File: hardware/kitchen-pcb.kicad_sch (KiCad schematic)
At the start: 51 parts, among them J1 MEM2075-00-140-01-A, J2 Conn_02x02_Odd_Even, J3 Conn_01x06, J4 S3B-XH-SM4-TB_LF__SN_, Q1 TEMT6000X01, U1 SHT30-DIS-B, U2 MX25L3233FM2I-08G

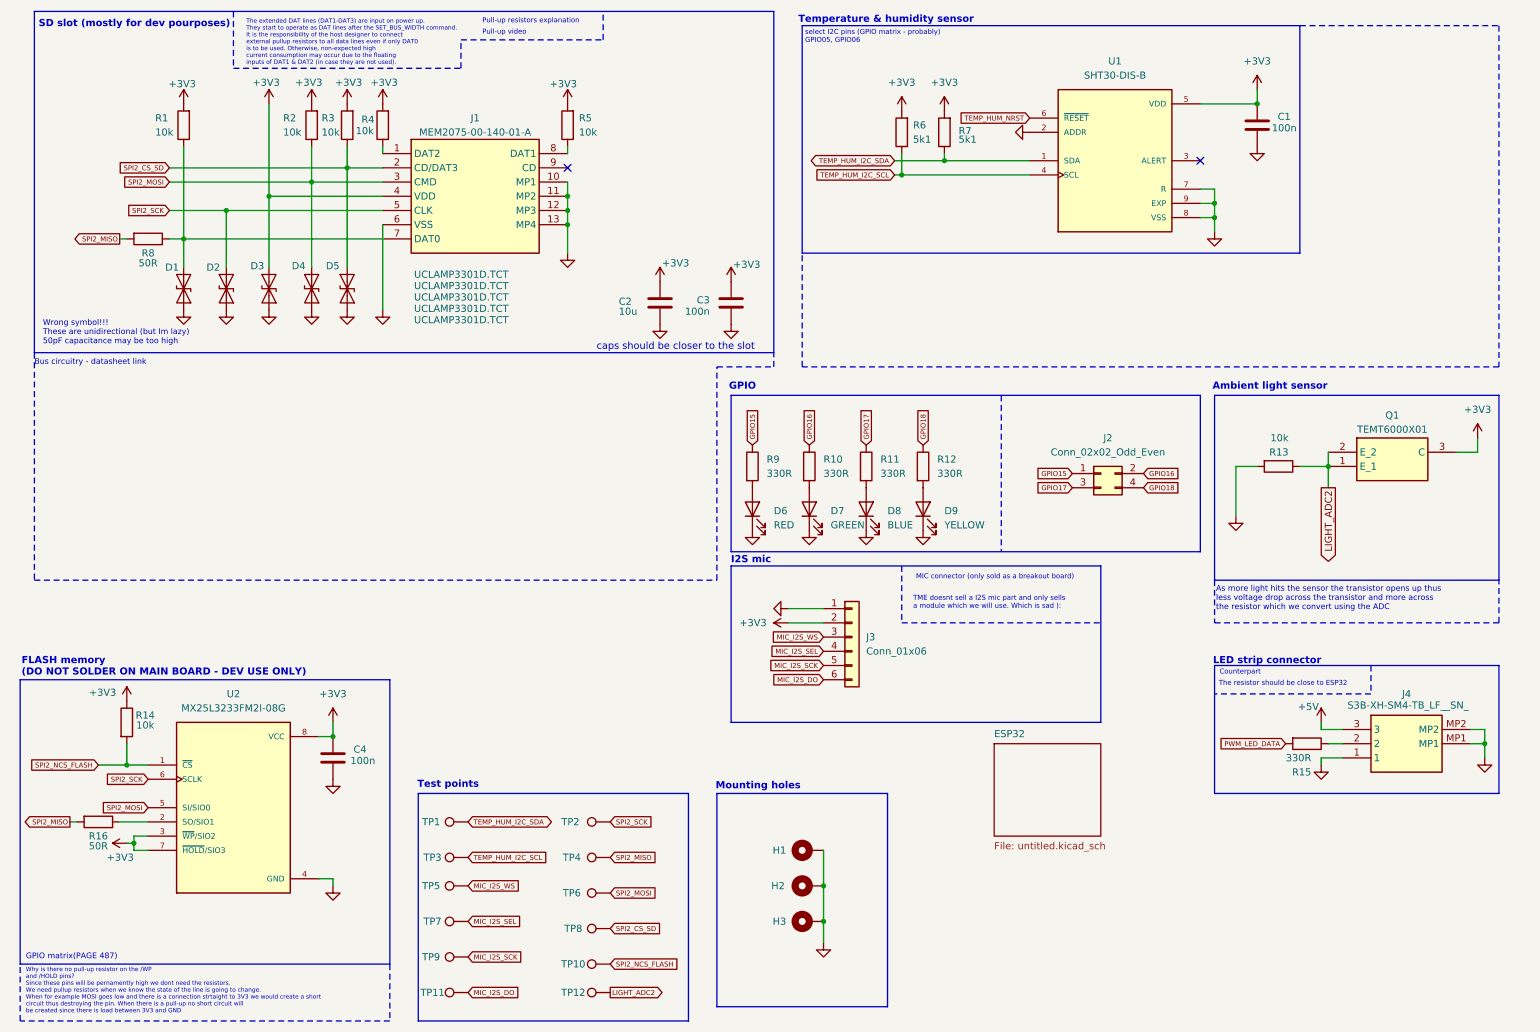
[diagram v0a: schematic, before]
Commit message: Tried to prevent crosstalk, fixed silkscreen, changes to fit DFM
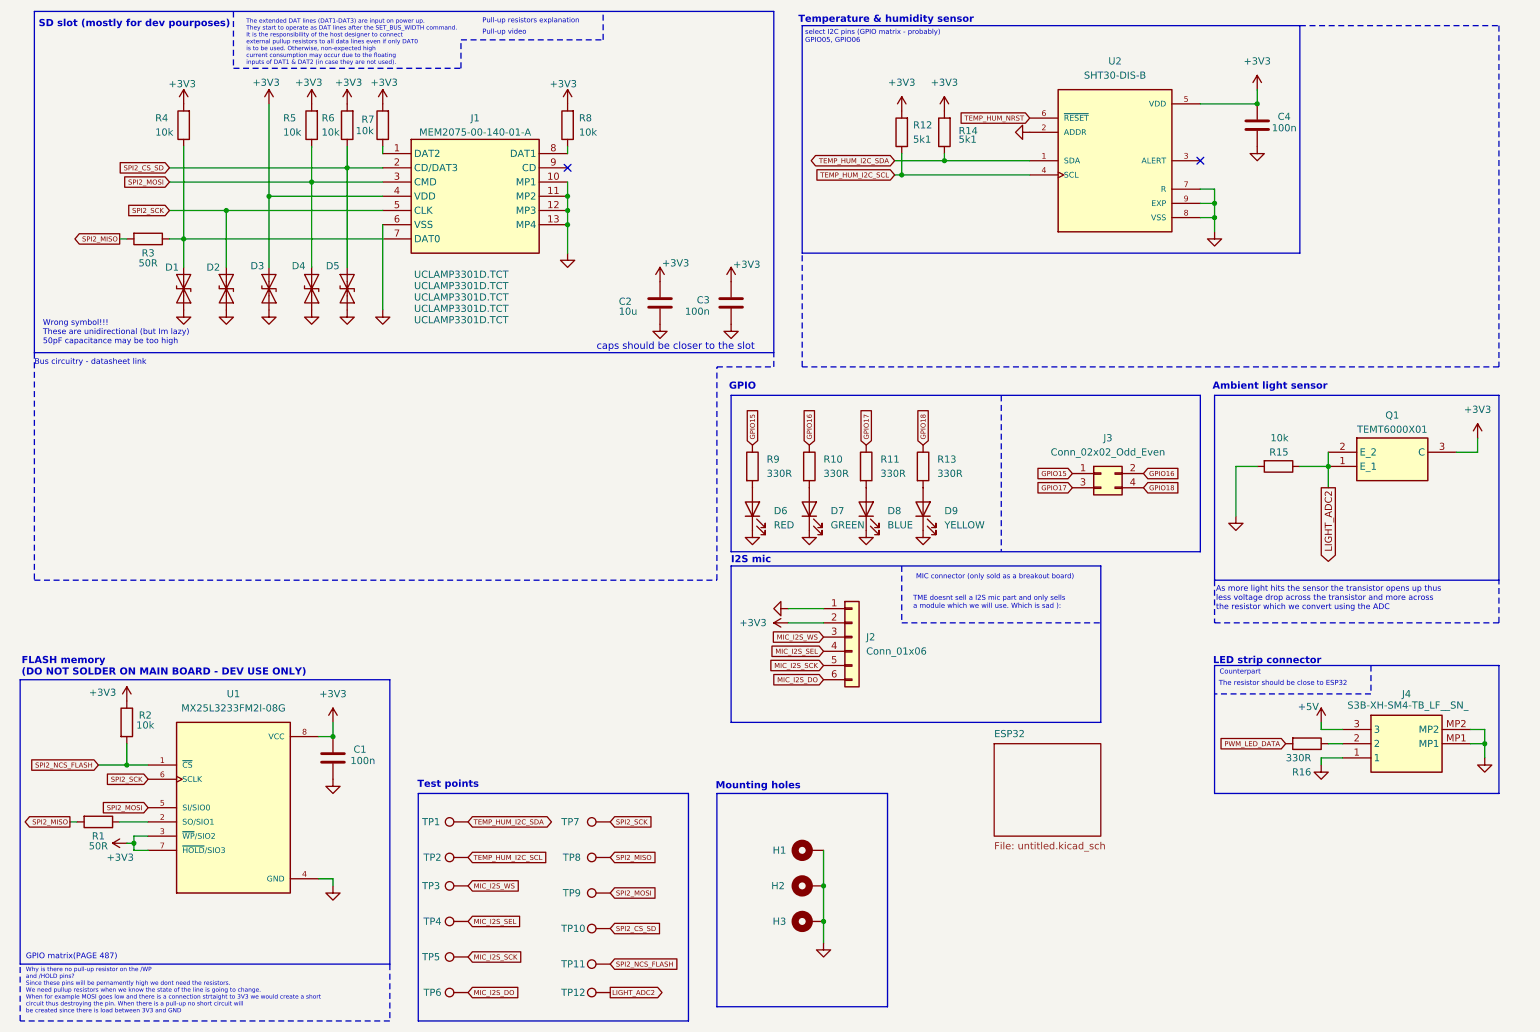
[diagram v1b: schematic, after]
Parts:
- renumbered C4 to C1, C1 to C4, J3 to J2, J2 to J3, R16 to R1, R6 to R12, R12 to R13, R7 to R14, R13 to R15, R15 to R16, R14 to R2, R8 to R3, R1 to R4, R2 to R5, R3 to R6, R4 to R7, R5 to R8, TP8 to TP10, TP10 to TP11, TP3 to TP2, TP5 to TP3, TP7 to TP4, TP9 to TP5, TP11 to TP6, TP2 to TP7, TP4 to TP8, TP6 to TP9, U2 to U1, U1 to U2
